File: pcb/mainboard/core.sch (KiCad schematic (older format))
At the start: 0 parts

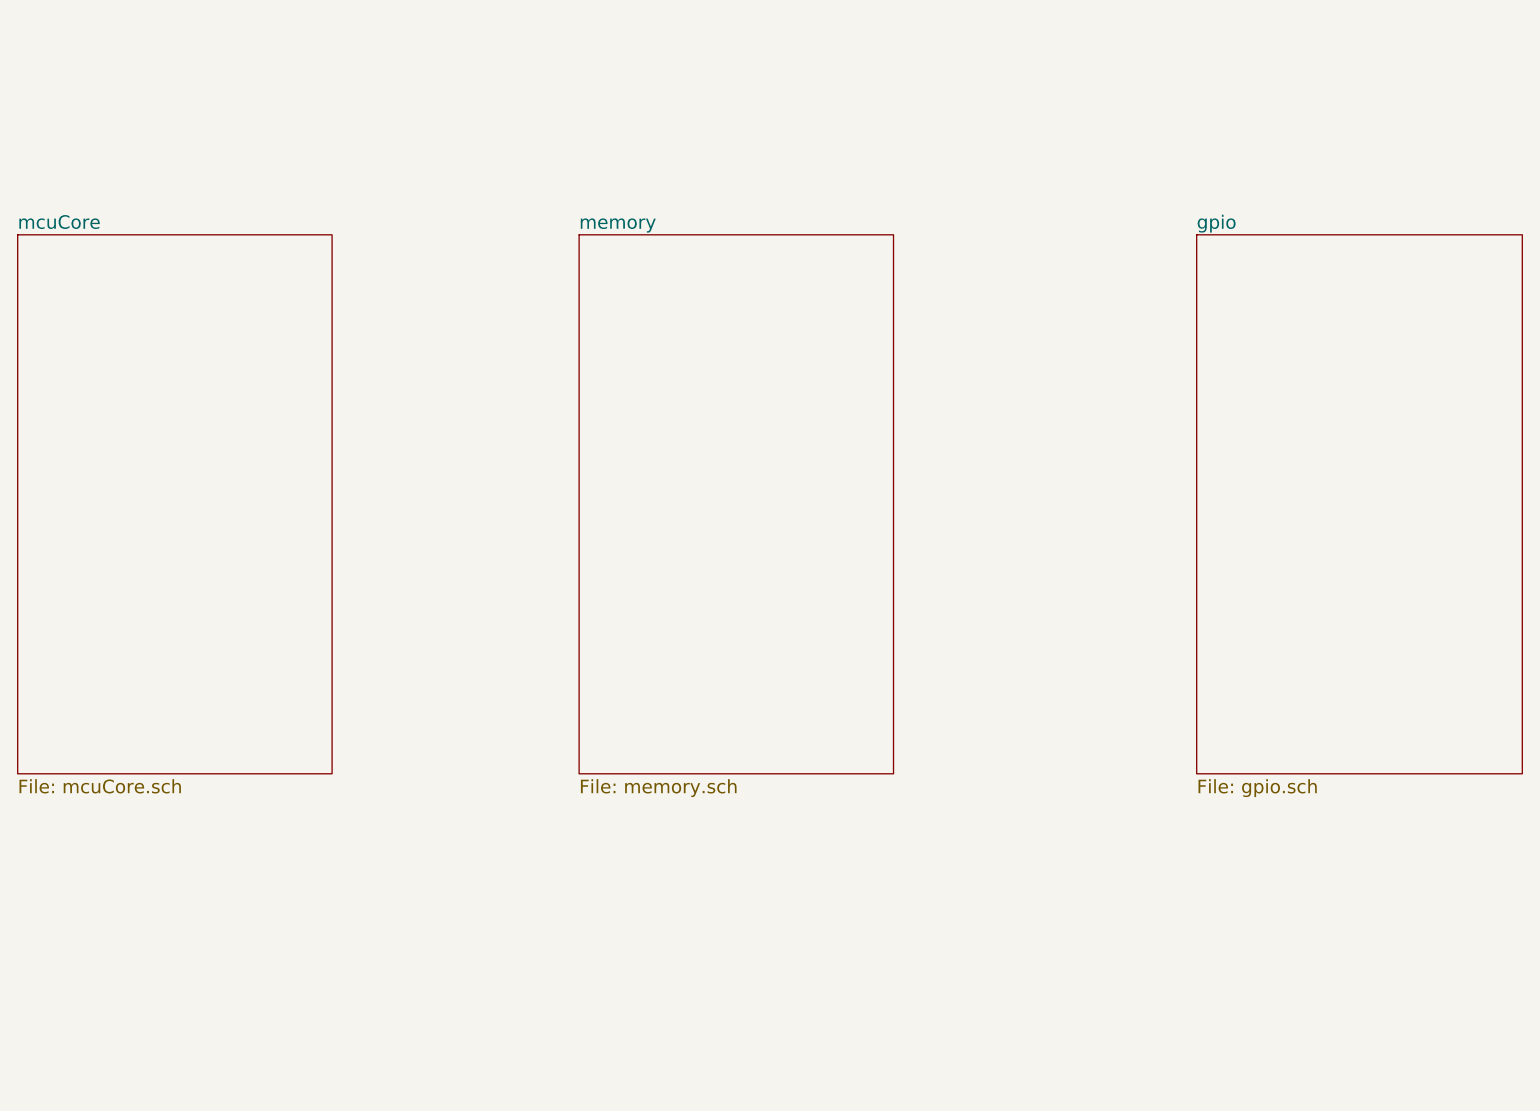
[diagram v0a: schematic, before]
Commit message: worked on PoE regulator
Added the SRAM
Added an EEPROM and a FLASH as nonvolatileMemory
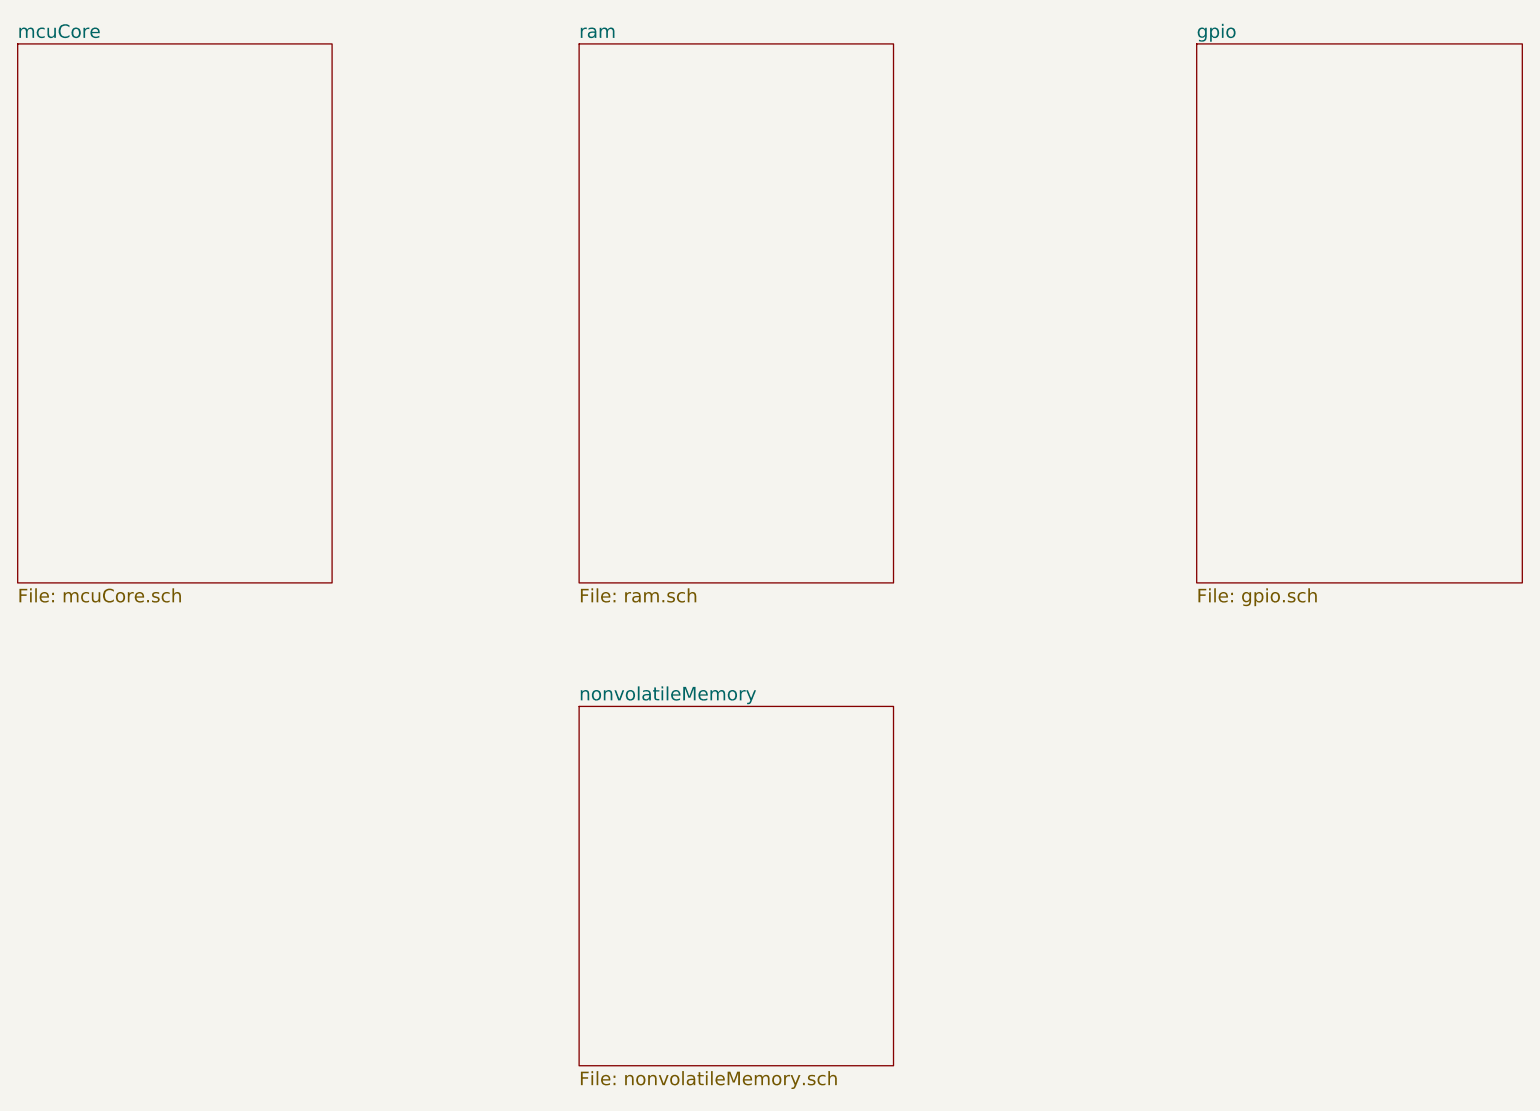
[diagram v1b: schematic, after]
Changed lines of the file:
@@
 $Descr A4 11693 8268
 encoding utf-8
-Sheet 3 9
-Title ""
+Sheet 2 10
+Title "ProzEthernatorMainboard"
 Date ""
-Rev ""
-Comp ""
+Rev "00"
+Comp "Shimatta"
 Comment1 ""
 Comment2 ""
@@
 $EndDescr
 $Sheet
-S 2000 2200 1400 2400
+S 2000 1350 1400 2400
 U 5A7CAB88
 F0 "mcuCore" 60
@@
 $EndSheet
 $Sheet
-S 4500 2200 1400 2400
+S 4500 1350 1400 2400
 U 5A7CAB8B
-F0 "memory" 60
-F1 "memory.sch" 60
+F0 "ram" 60
+F1 "ram.sch" 60
 $EndSheet
 $Sheet
-S 7250 2200 1450 2400
+S 7250 1350 1450 2400
 U 5A7CAB8E
 F0 "gpio" 60
 F1 "gpio.sch" 60
 $EndSheet
+$Sheet
+S 4500 4300 1400 1600
+U 5A866919
+F0 "nonvolatileMemory" 60
+F1 "nonvolatileMemory.sch" 60
+$EndSheet
 $EndSCHEMATC
